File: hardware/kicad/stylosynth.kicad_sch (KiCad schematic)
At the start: 101 parts, among them J1 9V DC (centre -), J2 9V BATT, J3 STYLUS, J4 PHONES, J5 SPEAKER, K1 KEYPAD, SW1 POWER, SW2 OCT -1, SW3 OCT -2, SW4 TONE, SW5 VIBRATO, U1 LP2950-5.0, U2 TLC555, U3 CD4040, U4 LM386, U5 LM358

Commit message: v1.1: piano-layout keyboard, fixed E96 ladder with TUNE/SPAN calibration, 170x108 board
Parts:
- removed RV101: 5k, Potentiometer_THT:Potentiometer_Bourns_3296W_Vertical, symbol Device:R_Potentiometer_Trim
- removed RV102, RV103, RV104, RV105, RV106, RV107, RV108, RV109, RV110, RV111, RV112, RV113, RV114, RV115, RV116, RV117, RV118, RV119, RV120: 1k, Potentiometer_THT:Potentiometer_Bourns_3296W_Vertical, symbol Device:R_Potentiometer_Trim
- added RV4: 2k, Potentiometer_THT:Potentiometer_Bourns_3296W_Vertical, symbol Device:R_Potentiometer_Trim
- added RV5: 1k, Potentiometer_THT:Potentiometer_Bourns_3296W_Vertical, symbol Device:R_Potentiometer_Trim
- R101: value 9.1k -> 11k3
- R102: value 220 -> 750
- R103: value 270 -> 787
- R104: value 300 -> 845
- R105: value 360 -> 887
- R106: value 430 -> 953
- R107: value 470 -> 1k
- R108: value 510 -> 1k05
- R109: value 560 -> 1k13
- R110: value 620 -> 1k18
- R111: value 680 -> 1k27
- R112: value 750 -> 1k33
- R113: value 820 -> 1k4
- R114: value 910 -> 1k5
- R115: value 1k -> 1k58
- R116: value 1.1k -> 1k69
- R117: value 1.2k -> 1k78
- R118: value 1.3k -> 1k87
- R119: value 1.3k -> 2k
- R120: value 1.5k -> 2k15
- R5: value 3k -> 2k4
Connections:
- net LAD1 is gone; now on net KEY19: R102.2
- net LAD10 is gone; now on net KEY10: R111.2
- net LAD11 is gone; now on net KEY9: R112.2
- net LAD12 is gone; now on net KEY8: R113.2
- net LAD13 is gone; now on net KEY7: R114.2
- net LAD14 is gone; now on net KEY6: R115.2
- net LAD15 is gone; now on net KEY5: R116.2
- net LAD16 is gone; now on net KEY4: R117.2
- net LAD17 is gone; now on net KEY3: R118.2
- net LAD18 is gone; now on net KEY2: R119.2
- net LAD19 is gone; now on net KEY1: R120.2
- net LAD2 is gone; now on net KEY18: R103.2
- net LAD3 is gone; now on net KEY17: R104.2
- net LAD4 is gone; now on net KEY16: R105.2
- net LAD5 is gone; now on net KEY15: R106.2
- net LAD6 is gone; now on net KEY14: R107.2
- net LAD7 is gone; now on net KEY13: R108.2
- net LAD8 is gone; now on net KEY12: R109.2
- net LAD9 is gone; now on net KEY11: R110.2
- net GND: now also RV5.2, RV5.3; no longer R5.2
- net KEY20: now also RV4.2, RV4.3
- net LAD0: now also RV4.1
- new net CV_LO: R5.2, RV5.1
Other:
- moved on the sheet: C8, H1, H2, H3, H4, H5, H6, J3, K1, R103, R104, R105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

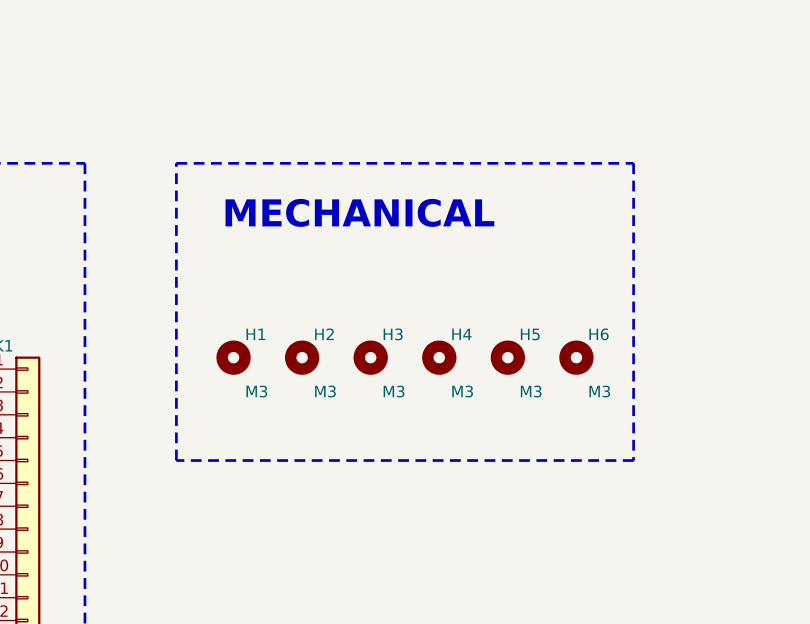
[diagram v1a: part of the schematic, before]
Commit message: v1.2: compact 136x98 layout, vertical resistors, single ladder row
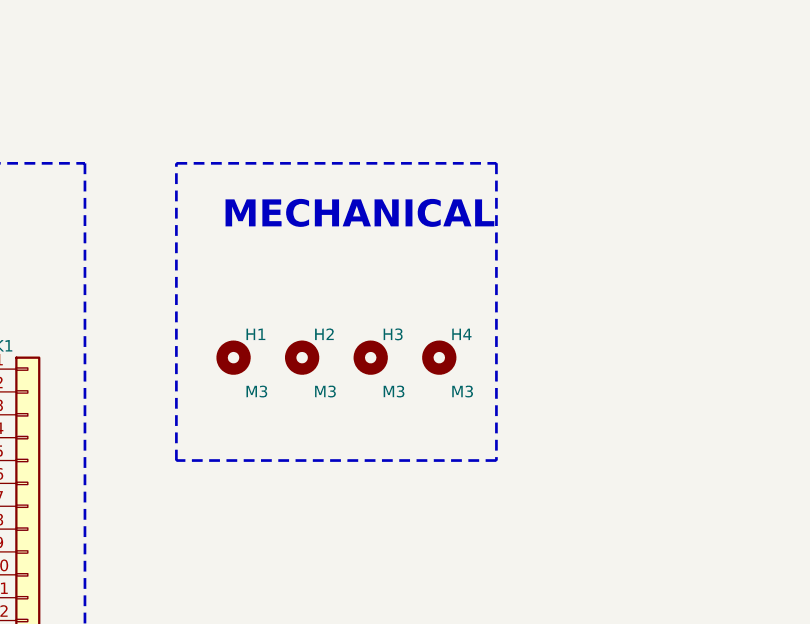
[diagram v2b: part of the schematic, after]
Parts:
- removed H5, H6: M3, MountingHole:MountingHole_3.2mm_M3, symbol Mechanical:MountingHole
- D1: footprint Diode_THT:D_DO-41_SOD81_P10.16mm_Horizontal -> Diode_THT:D_DO-41_SOD81_P5.08mm_Vertical_KathodeUp
- R1, R10, R11, R12, R13, R14, R2, R3, R4, R5, R6, R7, R8, R9: footprint Resistor_THT:R_Axial_DIN0207_L6.3mm_D2.5mm_P7.62mm_Horizontal -> Resistor_THT:R_Axial_DIN0207_L6.3mm_D2.5mm_P2.54mm_Vertical
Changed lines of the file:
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@@
       )
     )
-    (property "Footprint" "Diode_THT:D_DO-41_SOD81_P10.16mm_Horizontal"
+    (property "Footprint" "Diode_THT:D_DO-41_SOD81_P5.08mm_Vertical_KathodeUp"
       (at 86.36 43.18 0)
       (effects
@@
       )
     )
-    (property "Footprint" "Resistor_THT:R_Axial_DIN0207_L6.3mm_D2.5mm_P7.62mm_Horizontal"
+    (property "Footprint" "Resistor_THT:R_Axial_DIN0207_L6.3mm_D2.5mm_P2.54mm_Vertical"
       (at 208.28 46.99 0)
       (effects
@@
       )
     )
-    (property "Footprint" "Resistor_THT:R_Axial_DIN0207_L6.3mm_D2.5mm_P7.62mm_Horizontal"
+    (property "Footprint" "Resistor_THT:R_Axial_DIN0207_L6.3mm_D2.5mm_P2.54mm_Vertical"
       (at 254 46.99 0)
       (effects
@@
       )
     )
-    (property "Footprint" "Resistor_THT:R_Axial_DIN0207_L6.3mm_D2.5mm_P7.62mm_Horizontal"
+    (property "Footprint" "Resistor_THT:R_Axial_DIN0207_L6.3mm_D2.5mm_P2.54mm_Vertical"
       (at 378.46 45.72 0)
       (effects
@@
       )
     )
-    (property "Footprint" "Resistor_THT:R_Axial_DIN0207_L6.3mm_D2.5mm_P7.62mm_Horizontal"
+    (property "Footprint" "Resistor_THT:R_Axial_DIN0207_L6.3mm_D2.5mm_P2.54mm_Vertical"
       (at 393.7 46.99 0)
       (effects
@@
       )
     )
-    (property "Footprint" "Resistor_THT:R_Axial_DIN0207_L6.3mm_D2.5mm_P7.62mm_Horizontal"
+    (property "Footprint" "Resistor_THT:R_Axial_DIN0207_L6.3mm_D2.5mm_P2.54mm_Vertical"
       (at 407.67 45.72 0)
       (effects
@@
       )
     )
-    (property "Footprint" "Resistor_THT:R_Axial_DIN0207_L6.3mm_D2.5mm_P7.62mm_Horizontal"
+    (property "Footprint" "Resistor_THT:R_Axial_DIN0207_L6.3mm_D2.5mm_P2.54mm_Vertical"
       (at 457.2 50.8 0)
       (effects
@@
       )
     )
-    (property "Footprint" "Resistor_THT:R_Axial_DIN0207_L6.3mm_D2.5mm_P7.62mm_Horizontal"
+    (property "Footprint" "Resistor_THT:R_Axial_DIN0207_L6.3mm_D2.5mm_P2.54mm_Vertical"
       (at 149.86 133.35 0)
       (effects
@@
       )
     )
-    (property "Footprint" "Resistor_THT:R_Axial_DIN0207_L6.3mm_D2.5mm_P7.62mm_Horizontal"
+    (property "Footprint" "Resistor_THT:R_Axial_DIN0207_L6.3mm_D2.5mm_P2.54mm_Vertical"
       (at 165.1 135.89 0)
       (effects
@@
       )
     )
-    (property "Footprint" "Resistor_THT:R_Axial_DIN0207_L6.3mm_D2.5mm_P7.62mm_Horizontal"
+    (property "Footprint" "Resistor_THT:R_Axial_DIN0207_L6.3mm_D2.5mm_P2.54mm_Vertical"
       (at 181.61 137.16 0)
       (effects
@@
       )
     )
-    (property "Footprint" "Resistor_THT:R_Axial_DIN0207_L6.3mm_D2.5mm_P7.62mm_Horizontal"
+    (property "Footprint" "Resistor_THT:R_Axial_DIN0207_L6.3mm_D2.5mm_P2.54mm_Vertical"
       (at 196.85 137.16 0)
       (effects
@@
       )
     )
-    (property "Footprint" "Resistor_THT:R_Axial_DIN0207_L6.3mm_D2.5mm_P7.62mm_Horizontal"
+    (property "Footprint" "Resistor_THT:R_Axial_DIN0207_L6.3mm_D2.5mm_P2.54mm_Vertical"
       (at 81.28 176.53 0)
       (effects
@@
       )
     )
-    (property "Footprint" "Resistor_THT:R_Axial_DIN0207_L6.3mm_D2.5mm_P7.62mm_Horizontal"
+    (property "Footprint" "Resistor_THT:R_Axial_DIN0207_L6.3mm_D2.5mm_P2.54mm_Vertical"
       (at 27.94 240.03 0)
       (effects
@@
       )
     )
-    (property "Footprint" "Resistor_THT:R_Axial_DIN0207_L6.3mm_D2.5mm_P7.62mm_Horizontal"
+    (property "Footprint" "Resistor_THT:R_Axial_DIN0207_L6.3mm_D2.5mm_P2.54mm_Vertical"
       (at 241.3 240.03 0)
       (effects
@@
       )
     )
-    (property "Footprint" "Resistor_THT:R_Axial_DIN0207_L6.3mm_D2.5mm_P7.62mm_Horizontal"
+    (property "Footprint" "Resistor_THT:R_Axial_DIN0207_L6.3mm_D2.5mm_P2.54mm_Vertical"
       (at 27.94 285.75 0)
       (effects
@@
   (rectangle
     (start 396.24 311.15)
-    (end 447.04 344.17)
+    (end 431.8 344.17)
     (stroke
       (width 0.3)
@@
           (unit 1)
         )
-      )
-    )
-  )
-  (symbol
-    (lib_id "Mechanical:MountingHole")
-    (at 433.07 332.74 0)
-    (unit 1)
-    (in_bom yes)
-    (on_board yes)
-    (dnp no)
-    (property "Reference" "H5"
-      (at 434.34 330.2 0)
-      (effects
-        (font
-          (size 1.27 1.27)
-        )
-        (justify left)
-      )
-    )
-    (property "Value" "M3"
-      (at 434.34 336.55 0)
-      (effects
-        (font
-          (size 1.27 1.27)
-        )
-        (justify left)
-      )
-    )
-    (property "Footprint" "MountingHole:MountingHole_3.2mm_M3"
-      (at 433.07 332.74 0)
-      (effects
-        (font
-          (size 1.27 1.27)
-        )
-        hide
-      )
-    )
-    (property "Datasheet" "~"
-      (at 433.07 332.74 0)
-      (effects
-        (font
-          (size 1.27 1.27)
-        )
-        hide
-      )
-    )
-    (property "Description" "Mounting hole M3"
-      (at 433.07 332.74 0)
-      (effects
-        (font
-          (size 1.27 1.27)
-        )
-        hide
-      )
-    )
-    (property "Block" "Mechanical"
-      (at 433.07 332.74 0)
-      (effects
-        (font
-          (size 1.27 1.27)
-        )
-        hide
-      )
-    )
-    (instances
-      (project "stylosynth"
-        (path "/8eaf78e7-0c0c-56c2-b79f-e596e7a8f251"
-          (reference "H5")
-          (unit 1)
-        )
-      )
-    )
-  )
-  (symbol
-    (lib_id "Mechanical:MountingHole")
-    (at 440.69 332.74 0)
-    (unit 1)
-    (in_bom yes)
-    (on_board yes)
-    (dnp no)
-    (property "Reference" "H6"
-      (at 441.96 330.2 0)
-      (effects
-        (font
-          (size 1.27 1.27)
-        )
-        (justify left)
-      )
-    )
-    (property "Value" "M3"
-      (at 441.96 336.55 0)
-      (effects
-        (font
-          (size 1.27 1.27)
-        )
-        (justify left)
-      )
-    )
-    (property "Footprint" "MountingHole:MountingHole_3.2mm_M3"
-      (at 440.69 332.74 0)
-      (effects
-        (font
-          (size 1.27 1.27)
-        )
-        hide
-      )
-    )
-    (property "Datasheet" "~"
-      (at 440.69 332.74 0)
-      (effects
-        (font
-          (size 1.27 1.27)
-        )
-        hide
-      )
-    )
-    (property "Description" "Mounting hole M3"
-      (at 440.69 332.74 0)
-      (effects
-        (font
-          (size 1.27 1.27)
-        )
-        hide
-      )
-    )
-    (property "Block" "Mechanical"
-      (at 440.69 332.74 0)
-      (effects
-        (font
-          (size 1.27 1.27)
-        )
-        hide
-      )
-    )
-    (instances
-      (project "stylosynth"
-        (path "/8eaf78e7-0c0c-56c2-b79f-e596e7a8f251"
-          (reference "H6")
-          (unit 1)
-        )
